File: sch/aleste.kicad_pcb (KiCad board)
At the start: 2 copper layers, 334 x 193 mm, 313 parts, among them P1 PIN, P2 PIN, P3 PIN, P4 PIN, P5 PIN, P6 PIN, P7 PIN, P8 PIN, Q1 16 MHz, Q2 13.333 MHz, Q3 QUARTZ, X1 SLOT-62, X2 CONN-7S, X3 CONN-5S, X4 SLOT-34, X5.A1 CONN-7S, X5.B1 CONN-7S, X6 CONN-7S, X7 CONN-7S, X8 CONN-12, X9 CONN-12

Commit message: More precise version. PCB needs a lot of work.
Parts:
- removed the CB1 at (45.7, 118.1)
- removed the CB1 at (316.2, 209.6)
- removed the CB1 at (316.2, 199.4)
- removed the CB1 at (316.2, 189.2)
- removed the CB1 at (316.2, 148.6)
- removed the CB1 at (316.2, 158.8)
- removed the CB1 at (316.2, 168.9)
- removed the CB1 at (316.2, 179.1)
- removed the CB1 at (341.6, 179.1)
- removed the CB1 at (341.6, 168.9)
- removed the CB1 at (341.6, 158.8)
- removed the CB1 at (92.7, 147.3)
- removed the CB1 at (341.6, 148.6)
- removed the CB1 at (341.6, 189.2)
- removed the CB1 at (341.6, 199.4)
- removed the CB1 at (341.6, 209.6)
- removed the CB1 at (341.6, 219.7)
- removed the CB1 at (290.8, 185.4)
- removed the CB1 at (44.5, 222.2)
- removed the CB1 at (38.1, 83.8)
- removed the CB1 at (110.5, 86.4)
- removed the CB1 at (44.5, 174.0)
- removed the CB1 at (38.1, 149.9)
- removed the CB1 at (145.4, 224.8)
- removed the CB1 at (294.6, 57.1)
- removed the CB1 at (309.9, 58.4)
- removed the CB1 at (256.5, 54.6)
- removed the CB1 at (243.8, 68.6)
- removed the CB1 at (316.2, 219.7)
- removed the P7 at (64.8, 118.1)
- removed the P7 at (64.8, 105.4)
- added CB1: CAP, MyLib_metric:C_Disc_D7.5_P2.5, F.Cu at (127.3, 86.1)
- added CB1: CAP, MyLib_metric:C_Disc_D7.5_P2.5, F.Cu at (331.0, 197.3)
- added CB1: CAP, MyLib_metric:C_Disc_D7.5_P2.5, F.Cu at (331.0, 187.3)
- added CB1: CAP, MyLib_metric:C_Disc_D7.5_P2.5, F.Cu at (331.0, 177.3)
- added CB1: CAP, MyLib_metric:C_Disc_D7.5_P2.5, F.Cu at (331.0, 167.3)
- added CB1: CAP, MyLib_metric:C_Disc_D7.5_P2.5, F.Cu at (331.0, 157.3)
- added CB1: CAP, MyLib_metric:C_Disc_D7.5_P2.5, F.Cu at (331.0, 147.3)
- added CB1: CAP, MyLib_metric:C_Disc_D7.5_P2.5, F.Cu at (356.0, 147.3)
- added CB1: CAP, MyLib_metric:C_Disc_D7.5_P2.5, F.Cu at (356.0, 157.3)
- added CB1: CAP, MyLib_metric:C_Disc_D7.5_P2.5, F.Cu at (356.0, 167.3)
- added CB1: CAP, MyLib_metric:C_Disc_D7.5_P2.5, F.Cu at (356.0, 177.3)
- added CB1: CAP, MyLib_metric:C_Disc_D7.5_P2.5, F.Cu at (56.0, 82.3)
- added CB1: CAP, MyLib_metric:C_Disc_D7.5_P2.5, F.Cu at (356.0, 187.3)
- added CB1: CAP, MyLib_metric:C_Disc_D7.5_P2.5, F.Cu at (356.0, 197.3)
- added CB1: CAP, MyLib_metric:C_Disc_D7.5_P2.5, F.Cu at (356.0, 207.3)
- added CB1: CAP, MyLib_metric:C_Disc_D7.5_P2.5, F.Cu at (356.0, 217.3)
- added CB1: CAP, MyLib_metric:C_Disc_D7.5_P2.5, F.Cu at (306.0, 184.8)
- added CB1: CAP, MyLib_metric:C_Disc_D7.5_P2.5, F.Cu at (259.8, 69.8)
- added CB1: CAP, MyLib_metric:C_Disc_D7.5_P2.5, F.Cu at (309.8, 57.3)
- added CB1: CAP, MyLib_metric:C_Disc_D7.5_P2.5, F.Cu at (324.8, 58.6)
- added CB1: CAP, MyLib_metric:C_Disc_D7.5_P2.5, F.Cu at (276.0, 172.3)
- added CB1: CAP, MyLib_metric:C_Disc_D7.5_P2.5, F.Cu at (162.3, 222.3)
- added CB1: CAP, MyLib_metric:C_Disc_D7.5_P2.5, F.Cu at (63.5, 117.3)
- added CB1: CAP, MyLib_metric:C_Disc_D7.5_P2.5, F.Cu at (62.3, 172.3)
- added CB1: CAP, MyLib_metric:C_Disc_D7.5_P2.5, F.Cu at (62.3, 222.3)
- added CB1: CAP, MyLib_metric:C_Disc_D7.5_P2.5, F.Cu at (113.5, 128.6)
- added CB1: CAP, MyLib_metric:C_Disc_D7.5_P2.5, F.Cu at (111.0, 146.1)
- added CB1: CAP, MyLib_metric:C_Disc_D7.5_P2.5, F.Cu at (56.0, 148.6)
- added CB1: CAP, MyLib_metric:C_Disc_D7.5_P2.5, F.Cu at (272.3, 54.8)
- added CB1: CAP, MyLib_metric:C_Disc_D7.5_P2.5, F.Cu at (331.0, 217.3)
- added CB1: CAP, MyLib_metric:C_Disc_D7.5_P2.5, F.Cu at (331.0, 207.3)
- added P7: PIN, MyLib:PIN, F.Cu at (82.3, 104.8)
- added P7: PIN, MyLib:PIN, F.Cu at (82.3, 117.3)
- added REF**: 1pin, Connect:1pin, F.Cu at (246.0, 51.1)
- added REF**: 1pin, Connect:1pin, F.Cu at (246.0, 221.1)
- added REF**: 1pin, Connect:1pin, F.Cu at (94.8, 221.1)
- added REF**: MountingHole_4-5mm, Mounting_Holes:MountingHole_4-5mm, F.Cu at (52.3, 46.1)
- C1, C2: value CAP -> 470; footprint MyLib:C_Disc_D7.5_P2.5 -> MyLib_metric:C_Disc_D7.5_P2.5
- C11, C12, C13, C15, C16, C17, C18, C23, C3, C4, C5, C7, C9: footprint MyLib:C_Disc_D7.5_P2.5 -> MyLib_metric:C_Disc_D7.5_P2.5
- D1, D10, D11, D12, D13, D14, D15, D16, D2, D20, D21, D22, D23, D24, D26, D28, D3, D32, D37, D38, D39, D4, D49, D5, D50, D51, D52, D53, D54, D55, D56, D59, D6, D63, D64, D67, D68, D69, D7, D74, D79, D8, D80, D81, D87, D88, D9: footprint MyLib:DIP-16 -> MyLib_metric:DIP-16
- D17, D18, D25, D30, D70: footprint MyLib:DIP-40 -> MyLib_metric:DIP-40
- D19, D33, D60, D61, D62, D65, D82, D83: footprint MyLib:DIP-24 -> MyLib_metric:DIP-24
- D29, D35, D36, D40, D41, D42, D43, D44, D57, D66, D71, D72, D73, D75, D76, D77, D78, D85: footprint MyLib:DIP-14 -> MyLib_metric:DIP-14
- D31, D34: footprint MyLib:DIP-28 -> MyLib_metric:DIP-28
- D45, D46, D47, D48, D58, D84, D89: footprint MyLib:DIP-20 -> MyLib_metric:DIP-20
- D86: footprint MyLib:DIP-8 -> MyLib_metric:DIP-8
- Q3: footprint MyLib:Crystal_Round_Vertical_5mm -> MyLib_metric:Crystal_Round_Vertical_5mm
- R1, R100, R105, R2, R3, R36, R4, R59, R60, R61: value RES -> 1.2K; footprint MyLib:Resistor_Horizontal_RM7.5mm -> MyLib_metric:Resistor_Horizontal_RM7.5mm
- R10, R106, R107, R108, R109, R11, R110, R111, R112, R113, R12, R13, R17, R18, R19, R20, R21, R22, R23, R28, R29, R30, R31, R32, R47, R48, R49, R50, R88, R89, R90, R91, R92, R93, R94, R95: footprint MyLib:Resistor_Vertical_RM2.5mm -> MyLib_metric:Resistor_Vertical_RM2.5mm
- R101, R102, R16, R57: value RES -> 360; footprint MyLib:Resistor_Horizontal_RM7.5mm -> MyLib_metric:Resistor_Horizontal_RM7.5mm
- R114, R115, R116, R117, R118, R119, R120, R121, R122: value RES -> 27; footprint MyLib:Resistor_Horizontal_RM7.5mm -> MyLib_metric:Resistor_Horizontal_RM7.5mm
- R123, R134, R136, R15, R35, R37, R38, R5, R52, R53, R54, R55, R58: footprint MyLib:Resistor_Horizontal_RM7.5mm -> MyLib_metric:Resistor_Horizontal_RM7.5mm
- R126, R127, R128, R131, R132, R133, R14, R25, R76, R82, R83, R84, R85, R86, R87: value RES -> 2K; footprint MyLib:Resistor_Horizontal_RM7.5mm -> MyLib_metric:Resistor_Horizontal_RM7.5mm
- R129: value RES -> 510; footprint MyLib:Resistor_Horizontal_RM7.5mm -> MyLib_metric:Resistor_Horizontal_RM7.5mm
- R130, R62, R63, R64, R66, R81: value RES -> 220; footprint MyLib:Resistor_Horizontal_RM7.5mm -> MyLib_metric:Resistor_Horizontal_RM7.5mm
- R135, R27, R33: value RES -> 10K; footprint MyLib:Resistor_Horizontal_RM7.5mm -> MyLib_metric:Resistor_Horizontal_RM7.5mm
- R24, R39, R40, R41, R42, R43, R44, R45, R46, R7, R77, R78, R79, R8, R80, R9: value RES -> 51; footprint MyLib:Resistor_Horizontal_RM7.5mm -> MyLib_metric:Resistor_Horizontal_RM7.5mm
- R26, R34: value RES -> 10k; footprint MyLib:Resistor_Horizontal_RM7.5mm -> MyLib_metric:Resistor_Horizontal_RM7.5mm
- R51: value RES -> 1.2k; footprint MyLib:Resistor_Horizontal_RM7.5mm -> MyLib_metric:Resistor_Horizontal_RM7.5mm
- R56, R65: value RES -> 120; footprint MyLib:Resistor_Horizontal_RM7.5mm -> MyLib_metric:Resistor_Horizontal_RM7.5mm
- R6: value RES -> 15K; footprint MyLib:Resistor_Horizontal_RM7.5mm -> MyLib_metric:Resistor_Horizontal_RM7.5mm
- R67, R68, R69, R70: value RES -> 2K; footprint MyLib:Resistor_Vertical_RM2.5mm -> MyLib_metric:Resistor_Vertical_RM2.5mm
- R71, R72, R73, R74, R75: value RES -> 1.2K; footprint MyLib:Resistor_Vertical_RM2.5mm -> MyLib_metric:Resistor_Vertical_RM2.5mm
- VD1, VD10, VD11, VD12, VD13, VD14, VD2, VD4, VD5, VD6, VD7, VD8, VD9: footprint MyLib:Diode_DO-35_SOD27_Horizontal_RM7.5 -> MyLib_metric:Diode_DO-35_SOD27_Horizontal_RM7.5
- X8, X9: footprint MyLib:FB-12 -> MyLib_metric:FB-12
- moved D30 42.0 mm to (182.3, 68.6)
- moved D25 40.9 mm to (258.5, 111.1)
- moved D70 40.1 mm to (313.5, 111.1)
- moved D31 34.7 mm to (174.8, 89.8)
- moved D17 33.8 mm to (142.3, 94.8)
- moved D33 32.1 mm to (113.5, 118.6)
- moved D34 31.9 mm to (361.0, 111.1)
- moved X9 30.3 mm to (237.3, 81.1)
- moved D63 27.1 mm to (72.3, 162.3)
- moved D64 26.7 mm to (94.8, 162.3)
- moved D78 26.2 mm to (122.3, 146.1)
- moved D77 26.2 mm to (122.3, 134.8)
- moved D24 26.0 mm to (209.8, 89.8)
- moved D39 25.7 mm to (253.5, 212.3)
- moved D37 25.6 mm to (253.5, 199.8)
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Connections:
- D18 pad 26: (no net) -> Net-(D18-Pad26)
- D18 pad 39: (no net) -> Net-(D18-Pad39)
- D19 pad 19: (no net) -> Net-(D19-Pad19)
- D19 pad 21: (no net) -> Net-(D19-Pad21)
- D19 pad 23: (no net) -> Net-(D19-Pad23)
- D24 pad 6: (no net) -> Net-(D24-Pad6)
- D25 pad 15: (no net) -> Net-(D25-Pad15)
- D25 pad 34: (no net) -> Net-(D25-Pad34)
- D25 pad 35: (no net) -> Net-(D25-Pad35)
- D34 pad 14: (no net) -> Net-(D34-Pad14)
- D34 pad 15: (no net) -> Net-(D34-Pad15)
- D34 pad 16: (no net) -> Net-(D34-Pad16)
- D34 pad 17: (no net) -> Net-(D34-Pad17)
- D34 pad 18: (no net) -> Net-(D34-Pad18)
- D34 pad 23: (no net) -> Net-(D34-Pad23)
- D37 pad 15: (no net) -> Net-(D37-Pad15)
- D37 pad 3: (no net) -> Net-(D37-Pad3)
- D37 pad 4: (no net) -> Net-(D37-Pad4)
- D37 pad 5: (no net) -> Net-(D37-Pad5)
- D37 pad 6: (no net) -> Net-(D37-Pad6)
- D39 pad 2: (no net) -> Net-(D39-Pad2)
- D39 pad 7: (no net) -> Net-(D39-Pad7)
- D40 pad 11: (no net) -> /RAM/MVI
- D40 pad 5: (no net) -> Net-(D40-Pad5)
- D49 pad 2: (no net) -> Net-(D49-Pad2)
- D49 pad 7: (no net) -> Net-(D49-Pad7)
- D50 pad 13: (no net) -> Net-(D50-Pad13)
- D50 pad 15: (no net) -> Net-(D50-Pad15)
- D50 pad 2: (no net) -> Net-(D50-Pad2)
- D50 pad 7: (no net) -> Net-(D50-Pad7)
- D51 pad 13: (no net) -> Net-(D51-Pad13)
- D51 pad 15: (no net) -> Net-(D51-Pad15)
- D51 pad 7: (no net) -> Net-(D51-Pad7)
- D54 pad 4: (no net) -> Net-(D54-Pad4)
- D54 pad 5: (no net) -> Net-(D54-Pad5)
- D54 pad 7: (no net) -> Net-(D54-Pad7)
- D56 pad 14: (no net) -> Net-(D56-Pad14)
- D56 pad 15: (no net) -> Net-(D56-Pad15)
- D57 pad 6: (no net) -> Net-(D57-Pad6)
- D57 pad 8: (no net) -> Net-(D57-Pad8)
- D58 pad 16: (no net) -> Net-(D58-Pad16)
- D58 pad 17: (no net) -> Net-(D58-Pad17)
- D58 pad 18: (no net) -> Net-(D58-Pad18)
- D58 pad 19: (no net) -> Net-(D58-Pad19)
- D60 pad 17: (no net) -> Net-(D60-Pad17)
- D60 pad 8: (no net) -> Net-(D60-Pad8)
- D61 pad 17: (no net) -> Net-(D61-Pad17)
- D61 pad 8: (no net) -> Net-(D61-Pad8)
- D62 pad 16: (no net) -> Net-(D62-Pad16)
- D63 pad 12: (no net) -> Net-(D63-Pad12)
- D63 pad 13: (no net) -> Net-(D63-Pad13)
- D63 pad 14: (no net) -> Net-(D63-Pad14)
- D64 pad 11: (no net) -> Net-(D64-Pad11)
- D65 pad 13: (no net) -> Net-(D65-Pad13)
- D69 pad 6: (no net) -> Net-(D69-Pad6)
- D69 pad 7: (no net) -> Net-(D69-Pad7)
- D69 pad 9: (no net) -> Net-(D69-Pad9)
- D70 pad 14: (no net) -> Net-(D70-Pad14)
- D70 pad 24: (no net) -> Net-(D70-Pad24)
- D70 pad 26: (no net) -> Net-(D70-Pad26)
- D70 pad 31: (no net) -> Net-(D70-Pad31)
- D70 pad 32: (no net) -> Net-(D70-Pad32)
- D70 pad 36: (no net) -> Net-(D70-Pad36)
- D71 pad 8: (no net) -> Net-(D71-Pad8)
- D74 pad 11: (no net) -> Net-(D74-Pad11)
- D74 pad 12: (no net) -> Net-(D74-Pad12)
- D74 pad 4: (no net) -> Net-(D74-Pad4)
- D74 pad 5: (no net) -> Net-(D74-Pad5)
- D74 pad 6: (no net) -> Net-(D74-Pad6)
- D77 pad 6: (no net) -> Net-(D77-Pad6)
- D79 pad 14: (no net) -> Net-(D79-Pad14)
- D79 pad 15: (no net) -> Net-(D79-Pad15)
- D81 pad 6: (no net) -> Net-(D81-Pad6)
- D88 pad 1: (no net) -> Net-(D88-Pad1)
- D88 pad 2: (no net) -> Net-(D88-Pad2)
- D88 pad 7: (no net) -> Net-(D88-Pad7)
- D88 pad 9: (no net) -> Net-(D88-Pad9)
- D89 pad 11: (no net) -> Net-(D89-Pad11)
- D89 pad 12: (no net) -> Net-(D89-Pad12)
- D89 pad 13: (no net) -> Net-(D89-Pad13)
- D89 pad 7: (no net) -> Net-(D89-Pad7)
- D89 pad 8: (no net) -> Net-(D89-Pad8)
- D89 pad 9: (no net) -> Net-(D89-Pad9)
- X1 pad B20: (no net) -> Net-(X1-PadB20)
- X1 pad B24: (no net) -> /~EXP
- X4 pad A1: (no net) -> Net-(X4-PadA1)
- X4 pad A17: (no net) -> Net-(X4-PadA17)
- X4 pad A2: (no net) -> Net-(X4-PadA2)
- X4 pad A3: (no net) -> Net-(X4-PadA3)
- X4 pad A7: (no net) -> Net-(X4-PadA7)
- X9 pad 10: (no net) -> Net-(X9-Pad10)
- X9 pad 11: (no net) -> Net-(X9-Pad11)
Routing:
- net GND: track 4808.9 -> 0.00 mm, vias 51 -> 0
- net VCC: track 3489.0 -> 0.00 mm, vias 37 -> 0
- net /CPU/~IOWR: track 727.8 -> 0.00 mm, vias 9 -> 0
- net /CPU/D3: track 648.1 -> 0.00 mm, vias 17 -> 0
- net /CPU/HY: track 639.2 -> 0.00 mm, vias 6 -> 0
- net /CPU/D4: track 630.6 -> 0.00 mm, vias 13 -> 0
- net /CPU/D0: track 599.5 -> 0.00 mm, vias 9 -> 0
- net /CPU/D1: track 598.1 -> 0.00 mm, vias 15 -> 0
- net /CPU/D2: track 572.5 -> 0.00 mm, vias 9 -> 0
- net /CPU/D6: track 550.3 -> 0.00 mm, vias 10 -> 0
- net /CPU/D7: track 548.0 -> 0.00 mm, vias 12 -> 0
- net /CPU/D5: track 530.0 -> 0.00 mm, vias 14 -> 0
- net /FDC/XD0: track 525.6 -> 0.00 mm, vias 7 -> 0
- net /CPU/~IORD: track 503.3 -> 0.00 mm, vias 9 -> 0
- net /CPU/A8: track 502.3 -> 0.00 mm, vias 10 -> 0
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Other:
- board size 334 x 193 mm -> 330 x 190 mm
- net class Default: via_dia 1 -> 1.2; via_drill 0.5 -> 0.8
- rule pad_to_mask_clearance: 0.2 -> 0
- board text removed: "Aleste 520EX"
- board text removed: "PATISONIC ALESTE 520 EX 01.003"
- board text removed: "designed by Patisonic, Omsk, 1992-1993 restored by Alexander Molodtsov, 2015"

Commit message: Board fully redrawn
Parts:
- C10, C14, C22: value CAPP -> 100мк
- C11: value CAP -> 12
- C12: value CAP -> 24
- C13: value CAP -> 47н
- C20: value CAPP -> 1000мк
- C23: value CAP -> 0,47мк
- C24, C6: value CAPP -> 1мк
- C25, C26: value CAPP -> 47мк
- C7: value CAP -> 0,33мк
- C9: value CAP -> 1,5мк
- CB1: value CAP -> 0,1мк
- DR1: value INDUCTOR -> 91мкГ
- DR2: value INDUCTOR -> 51мкГ
- R1, R100, R105, R2, R3, R36, R4, R60, R71, R72, R73, R74, R75: value 1.2K -> 1,2к
- R10, R11, R12, R13, R28, R29, R30, R31, R32, R47, R48, R49, R50: value RES -> 1,2к
- R106, R107, R108, R109, R110, R111, R112, R113, R17, R18, R19, R20, R21, R22, R23, R88, R89, R90, R91, R92, R93, R94, R95: value RES -> 10к
- R123, R15, R5: value RES -> 2,7к
- R126, R132, R14, R25, R67, R68, R69, R70, R76, R82, R83, R84, R85, R86, R87: value 2K -> 2,7к
- R127, R131: value 2K -> 6,8к
- R128, R133: value 2K -> 3,3к
- R134, R53, R55: value RES -> 360
- R135, R27, R33: value 10K -> 10к
- R35: value RES -> 390к
- R37: value RES -> 10М
- R38: value RES -> 470к
- R51: value 1.2k -> 1,2к
- R52, R54: value RES -> 200
- R56: value 120 -> 200
- R58: value RES -> 510
- R59: value 1.2K -> 6,8к
- R6: value 15K -> 2,7к
- R61: value 1.2K -> 3,3к
- moved C26 2.50 mm to (352.3, 77.3)
- moved CB1 2.50 mm to (62.3, 219.8)
- moved D59 2.50 mm to (62.3, 207.3)
- moved CB1 2.25 mm to (304.1, 183.6)
- moved CB1 2.25 mm to (111.6, 129.8)
- moved D45 2.25 mm to (296.6, 199.8)
- moved D46 2.25 mm to (311.6, 199.8)
- moved D47 2.25 mm to (296.6, 167.3)
- moved D48 2.25 mm to (311.6, 167.3)
- moved R77 2.25 mm to (311.6, 219.8)
- moved R78 2.25 mm to (296.6, 214.8)
- moved R79 2.25 mm to (296.6, 217.3)
- moved R8 2.25 mm to (311.6, 214.8)
- moved R80 2.25 mm to (296.6, 219.8)
- moved R9 2.25 mm to (311.6, 217.3)
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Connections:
- net /CPU/A0 renamed /A0
- net /CPU/A1 renamed /A1
- net /CPU/A10 renamed /A10
- net /CPU/A11 renamed /A11
- net /CPU/A12 renamed /A12
- net /CPU/A13 renamed /A13
- net /CPU/A14 renamed /A14
- net /CPU/A15 renamed /A15
- net /CPU/A2 renamed /A2
- net /CPU/A3 renamed /A3
- net /CPU/A4 renamed /A4
- net /CPU/A5 renamed /A5
- net /CPU/A6 renamed /A6
- net /CPU/A7 renamed /A7
- net /CPU/A8 renamed /A8
- net /CPU/A9 renamed /A9
- net /CPU/BUFFER0 renamed /BUFFER0
- net /CPU/BUFFER1 renamed /BUFFER1
- net /CPU/CLK renamed /CLK
- net /CPU/D0 renamed /D0
- net /CPU/D1 renamed /D1
- net /CPU/D2 renamed /D2
- net /CPU/D3 renamed /D3
- net /CPU/D4 renamed /D4
- net /CPU/D5 renamed /D5
- net /CPU/D6 renamed /D6
- net /CPU/D7 renamed /D7
- net /CPU/HY renamed /HY
- net /CPU/PROM0 renamed /PROM0
- net /CPU/PROM1 renamed /PROM1
- net /CPU/RAMDIS renamed /RAMDIS
- net /CPU/ROM0 renamed /ROM0
- net /CPU/ROM1 renamed /ROM1
- net /CPU/ROMDIS renamed /ROMDIS
- net /CPU/SINT renamed /SINT
- net /CPU/~BUSAK renamed /~BUSAK
- net /CPU/~BUSRQ renamed /~BUSRQ
- net /CPU/~HALT renamed /~HALT
- net /CPU/~INT renamed /~INT
- net /CPU/~INTA renamed /~INTA
- net /CPU/~IORD renamed /~IORD
- net /CPU/~IORQ renamed /~IORQ
- net /CPU/~IOWR renamed /~IOWR
- net /CPU/~M1 renamed /~M1
- net /CPU/~MREQ renamed /~MREQ
- net /CPU/~NMI renamed /~NMI
- net /CPU/~RAMEN renamed /~RAMEN
- net /CPU/~RD renamed /~RD
- net /CPU/~RESET renamed /~RESET
- net /CPU/~RFSH renamed /~RFSH
- net /CPU/~ROMEN renamed /~ROMEN
- net /CPU/~WAIT renamed /~WAIT
- net /CPU/~WR renamed /~WR
- net /Clocks & CRTC/16MHZ renamed /16MHZ
- net /Clocks & CRTC/1CY renamed /1CY
- net /Clocks & CRTC/1M renamed /1M
- net /Clocks & CRTC/2CY renamed /2CY
- net /Clocks & CRTC/2M renamed /2M
- net /Clocks & CRTC/3CY renamed /3CY
- net /Clocks & CRTC/4M renamed /4M
- net /Clocks & CRTC/8M renamed /8M
- net /Clocks & CRTC/CAS renamed /CAS
- net /Clocks & CRTC/CBUF renamed /CBUF
- net /Clocks & CRTC/CURSOR renamed /CURSOR
- net /Clocks & CRTC/DEN renamed /DEN
- net /Clocks & CRTC/HIGHT renamed /HIGHT
- net /Clocks & CRTC/HX renamed /HX
- net /Clocks & CRTC/HY* renamed /HY*
- net /Clocks & CRTC/KK0 renamed /KK0
- net /Clocks & CRTC/KK1 renamed /KK1
- net /Clocks & CRTC/KK2 renamed /KK2
- net /Clocks & CRTC/KK3 renamed /KK3
- net /Clocks & CRTC/L.PEN renamed /L.PEN
- net /Clocks & CRTC/L0 renamed /L0
- net /Clocks & CRTC/L1 renamed /L1
- net /Clocks & CRTC/L2 renamed /L2
- net /Clocks & CRTC/MK0 renamed /MK0
- net /Clocks & CRTC/MK1 renamed /MK1
- net /Clocks & CRTC/MK2 renamed /MK2
- net /Clocks & CRTC/MK3 renamed /MK3
- net /Clocks & CRTC/RAS renamed /RAS
- net /Clocks & CRTC/SINT* renamed /SINT*
- net /Clocks & CRTC/SYNC* renamed /SYNC*
- net /Clocks & CRTC/V1 renamed /V1
- net /Clocks & CRTC/V10 renamed /V10
- net /Clocks & CRTC/V1113 renamed /V1113
- net /Clocks & CRTC/V14 renamed /V14
- net /Clocks & CRTC/V2 renamed /V2
- net /Clocks & CRTC/V3 renamed /V3
- net /Clocks & CRTC/V4 renamed /V4
- net /Clocks & CRTC/V5 renamed /V5
- net /Clocks & CRTC/V6 renamed /V6
- net /Clocks & CRTC/V7 renamed /V7
- net /Clocks & CRTC/V8 renamed /V8
- net /Clocks & CRTC/V9 renamed /V9
- net /Clocks & CRTC/VCLK renamed /VCLK
- net /Clocks & CRTC/XTAL renamed /XTAL
- net /Clocks & CRTC/~3CY renamed /~3CY
- net /FDC/DISCINT renamed /DISCINT
- net /FDC/DW renamed /DW
- net /FDC/EXRG renamed /EXRG
- net /FDC/RESET renamed /RESET
- net /FDC/RSCLK renamed /RSCLK
- net /FDC/WGPTCLK renamed /WGPTCLK
- net /FDC/XD0 renamed /XD0
- net /Gate Array/CS53 renamed /CS53
- net /Gate Array/HIGHTZ renamed /HIGHTZ
- net /Gate Array/M4 renamed /M4
- net /Gate Array/MAP14 renamed /MAP14
- net /Gate Array/MAP15 renamed /MAP15
- net /Gate Array/MAP16 renamed /MAP16
- net /Gate Array/MAP17 renamed /MAP17
- net /Gate Array/MAP18 renamed /MAP18
- net /Gate Array/MAPBLK renamed /MAPBLK
- net /Gate Array/SOUND renamed /SOUND
- net /Gate Array/VD0 renamed /VD0
- net /Gate Array/VD1 renamed /VD1
- net /Gate Array/VD2 renamed /VD2
- net /Gate Array/VD3 renamed /VD3
- net /Gate Array/VD4 renamed /VD4
- net /Gate Array/VD5 renamed /VD5
- net /Gate Array/VD6 renamed /VD6
- net /Gate Array/VD7 renamed /VD7
- net /Gate Array/~CSAY renamed /~CSAY
- net /Gate Array/~FUTURE renamed /~FUTURE
- net /RAM/DIS renamed /DIS
- net /RAM/~DIS renamed /~DIS
- D18 pad 26: Net-(D18-Pad26) -> (no net)
- D18 pad 39: Net-(D18-Pad39) -> (no net)
- D19 pad 19: Net-(D19-Pad19) -> (no net)
- D19 pad 21: Net-(D19-Pad21) -> (no net)
- D19 pad 23: Net-(D19-Pad23) -> (no net)
- D24 pad 6: Net-(D24-Pad6) -> (no net)
- D25 pad 15: Net-(D25-Pad15) -> (no net)
- D25 pad 34: Net-(D25-Pad34) -> (no net)
- D25 pad 35: Net-(D25-Pad35) -> (no net)
- D34 pad 14: Net-(D34-Pad14) -> (no net)
- D34 pad 15: Net-(D34-Pad15) -> (no net)
- D34 pad 16: Net-(D34-Pad16) -> (no net)
- D34 pad 17: Net-(D34-Pad17) -> (no net)
- D34 pad 18: Net-(D34-Pad18) -> (no net)
- D34 pad 23: Net-(D34-Pad23) -> (no net)
- D35 pad 6: /Gate Array/MVI -> /MVI
- D37 pad 15: Net-(D37-Pad15) -> (no net)
- D37 pad 3: Net-(D37-Pad3) -> (no net)
- D37 pad 4: Net-(D37-Pad4) -> (no net)
- D37 pad 5: Net-(D37-Pad5) -> (no net)
- D37 pad 6: Net-(D37-Pad6) -> (no net)
- D39 pad 2: Net-(D39-Pad2) -> (no net)
- D39 pad 7: Net-(D39-Pad7) -> (no net)
- D40 pad 11: /RAM/MVI -> /MVI
- D40 pad 5: Net-(D40-Pad5) -> (no net)
- D49 pad 10: /Gate Array/MVI -> /MVI
- D49 pad 2: Net-(D49-Pad2) -> (no net)
- D49 pad 7: Net-(D49-Pad7) -> (no net)
- D49 pad 9: /Gate Array/MVI -> /MVI
- D50 pad 10: /Gate Array/MVI -> /MVI
- D50 pad 13: Net-(D50-Pad13) -> (no net)
- D50 pad 15: Net-(D50-Pad15) -> (no net)
- D50 pad 2: Net-(D50-Pad2) -> (no net)
- D50 pad 7: Net-(D50-Pad7) -> (no net)
- D51 pad 10: /Gate Array/MVI -> /MVI
- D51 pad 13: Net-(D51-Pad13) -> (no net)
- D51 pad 15: Net-(D51-Pad15) -> (no net)
- D51 pad 7: Net-(D51-Pad7) -> (no net)
- D54 pad 4: Net-(D54-Pad4) -> (no net)
- D54 pad 5: Net-(D54-Pad5) -> (no net)
- D54 pad 7: Net-(D54-Pad7) -> (no net)
- D56 pad 14: Net-(D56-Pad14) -> (no net)
- D56 pad 15: Net-(D56-Pad15) -> (no net)
- D57 pad 6: Net-(D57-Pad6) -> (no net)
- D57 pad 8: Net-(D57-Pad8) -> (no net)
- D58 pad 16: Net-(D58-Pad16) -> (no net)
- D58 pad 17: Net-(D58-Pad17) -> (no net)
- D58 pad 18: Net-(D58-Pad18) -> (no net)
- D58 pad 19: Net-(D58-Pad19) -> (no net)
- D60 pad 17: Net-(D60-Pad17) -> (no net)
- D60 pad 8: Net-(D60-Pad8) -> (no net)
- D61 pad 17: Net-(D61-Pad17) -> (no net)
- D61 pad 8: Net-(D61-Pad8) -> (no net)
- D62 pad 16: Net-(D62-Pad16) -> (no net)
- D63 pad 12: Net-(D63-Pad12) -> (no net)
- D63 pad 13: Net-(D63-Pad13) -> (no net)
- D63 pad 14: Net-(D63-Pad14) -> (no net)
- D64 pad 11: Net-(D64-Pad11) -> (no net)
- D65 pad 13: Net-(D65-Pad13) -> (no net)
- D69 pad 6: Net-(D69-Pad6) -> (no net)
- D69 pad 7: Net-(D69-Pad7) -> (no net)
- D69 pad 9: Net-(D69-Pad9) -> (no net)
- D70 pad 14: Net-(D70-Pad14) -> (no net)
- D70 pad 24: Net-(D70-Pad24) -> (no net)
- D70 pad 26: Net-(D70-Pad26) -> (no net)
- D70 pad 31: Net-(D70-Pad31) -> (no net)
- D70 pad 32: Net-(D70-Pad32) -> (no net)
- D70 pad 36: Net-(D70-Pad36) -> (no net)
- D71 pad 8: Net-(D71-Pad8) -> (no net)
- D74 pad 11: Net-(D74-Pad11) -> (no net)
- D74 pad 12: Net-(D74-Pad12) -> (no net)
- D74 pad 4: Net-(D74-Pad4) -> (no net)
- D74 pad 5: Net-(D74-Pad5) -> (no net)
- D74 pad 6: Net-(D74-Pad6) -> (no net)
- D77 pad 6: Net-(D77-Pad6) -> (no net)
- D79 pad 14: Net-(D79-Pad14) -> (no net)
- D79 pad 15: Net-(D79-Pad15) -> (no net)
- D81 pad 6: Net-(D81-Pad6) -> (no net)
- D88 pad 1: Net-(D88-Pad1) -> (no net)
- D88 pad 2: Net-(D88-Pad2) -> (no net)
- D88 pad 7: Net-(D88-Pad7) -> (no net)
- D88 pad 9: Net-(D88-Pad9) -> (no net)
- D89 pad 11: Net-(D89-Pad11) -> (no net)
- D89 pad 12: Net-(D89-Pad12) -> (no net)
- D89 pad 13: Net-(D89-Pad13) -> (no net)
- D89 pad 7: Net-(D89-Pad7) -> (no net)
- D89 pad 8: Net-(D89-Pad8) -> (no net)
- D89 pad 9: Net-(D89-Pad9) -> (no net)
- R76 pad 1: VCC -> Net-(D70-Pad15)
- R76 pad 2: Net-(D70-Pad15) -> VCC
- X1 pad B20: Net-(X1-PadB20) -> (no net)
- X1 pad B24: /~EXP -> (no net)
- X4 pad A1: Net-(X4-PadA1) -> (no net)
- X4 pad A17: Net-(X4-PadA17) -> (no net)
- X4 pad A2: Net-(X4-PadA2) -> (no net)
- X4 pad A3: Net-(X4-PadA3) -> (no net)
- X4 pad A7: Net-(X4-PadA7) -> (no net)
- X9 pad 10: Net-(X9-Pad10) -> (no net)
- X9 pad 11: Net-(X9-Pad11) -> (no net)
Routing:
- net GND: track 0.00 -> 4144.7 mm, vias 0 -> 47
- net VCC: track 0.00 -> 3431.0 mm, vias 0 -> 30
- net /D3: track 0.00 -> 647.9 mm, vias 0 -> 17
- net /D4: track 0.00 -> 621.7 mm, vias 0 -> 13
- net /D1: track 0.00 -> 589.3 mm, vias 0 -> 15
- net /D0: track 0.00 -> 588.6 mm, vias 0 -> 9
- net /D2: track 0.00 -> 563.6 mm, vias 0 -> 9
- net /D7: track 0.00 -> 544.8 mm, vias 0 -> 12
- net /D6: track 0.00 -> 541.9 mm, vias 0 -> 10
- net /D5: track 0.00 -> 534.6 mm, vias 0 -> 14
- net /XD0: track 0.00 -> 528.3 mm, vias 0 -> 7
- net /~IOWR: track 0.00 -> 527.2 mm, vias 0 -> 9
- net /~IORD: track 0.00 -> 492.9 mm, vias 0 -> 9
- net /A8: track 0.00 -> 492.2 mm, vias 0 -> 10
- net /A0: track 0.00 -> 415.2 mm, vias 0 -> 11
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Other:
- board size 330 x 190 mm -> 328.8 x 190 mm
- board text added: "Aleste 520EX"
- board text added: "TIN"
- board text added: "TOUT"
- board text added: "WGPTCLK"
- board text added: "designed by Patisonic, Omsk, 1992-1993"
- board text added: "restored by Alexander Molodtsov, 2015"

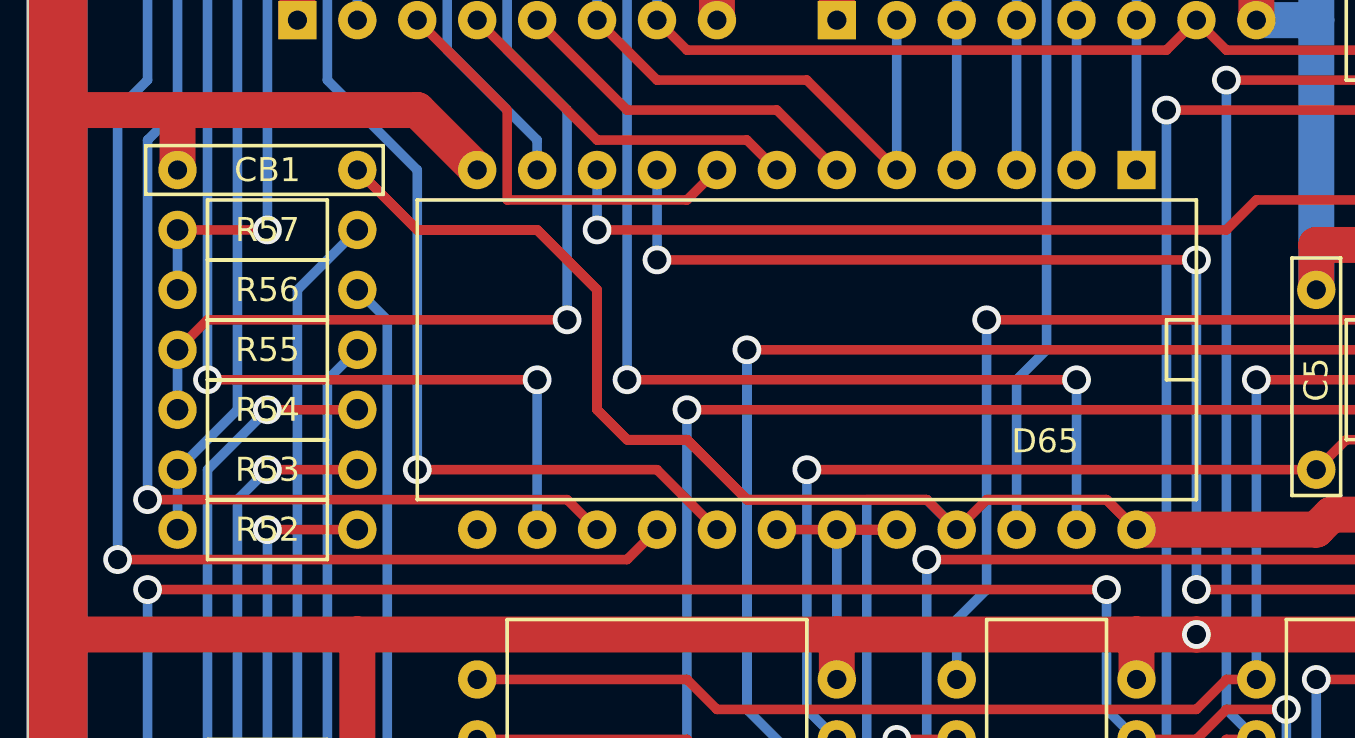
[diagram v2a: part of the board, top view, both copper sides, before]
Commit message: C8 on its place
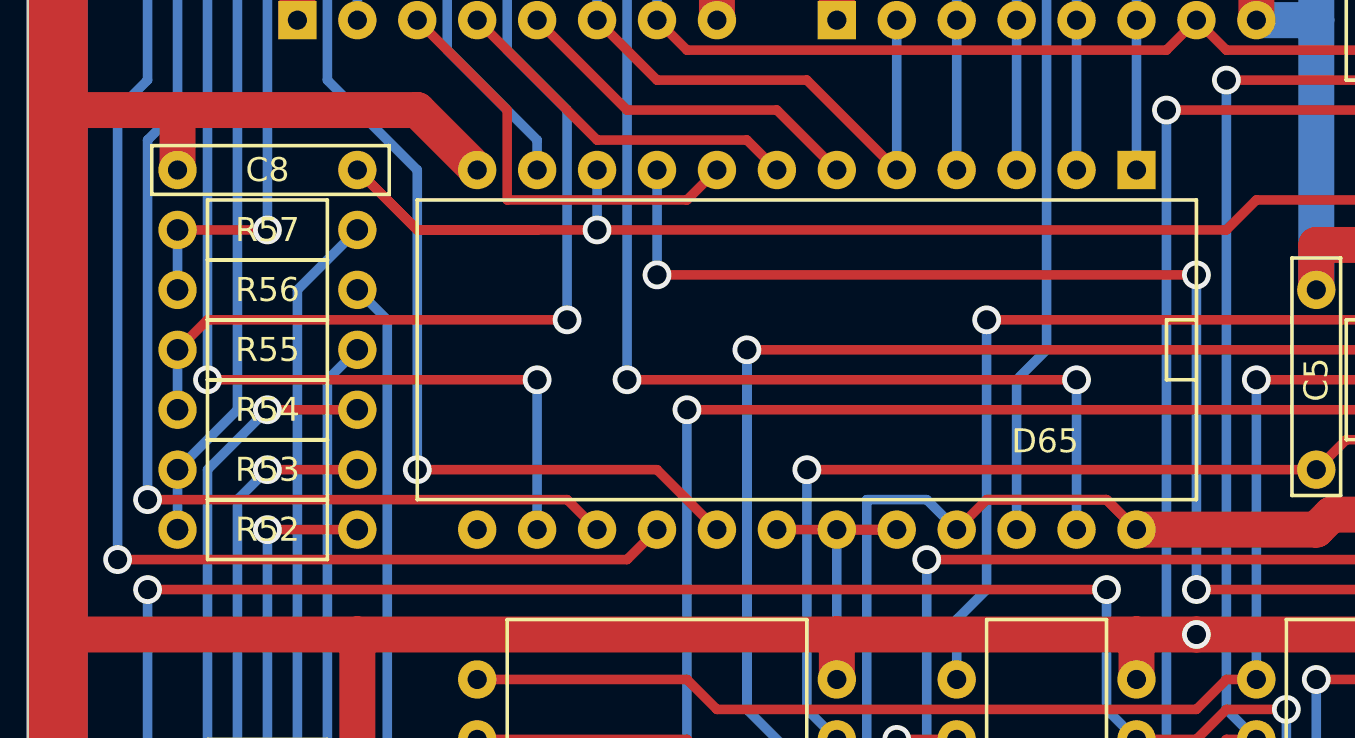
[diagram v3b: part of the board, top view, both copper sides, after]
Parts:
- C8: renamed from CB1; value CAP -> 1н
- turned C8 to 180 degrees
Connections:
- C8 pad 1: GND -> /HY*
- C8 pad 2: VCC -> GND
- D18 pad 26: (no net) -> Net-(D18-Pad26)
- D18 pad 39: (no net) -> Net-(D18-Pad39)
- D19 pad 19: (no net) -> Net-(D19-Pad19)
- D19 pad 21: (no net) -> Net-(D19-Pad21)
- D19 pad 23: (no net) -> Net-(D19-Pad23)
- D24 pad 6: (no net) -> Net-(D24-Pad6)
- D25 pad 15: (no net) -> Net-(D25-Pad15)
- D25 pad 34: (no net) -> Net-(D25-Pad34)
- D25 pad 35: (no net) -> Net-(D25-Pad35)
- D34 pad 14: (no net) -> Net-(D34-Pad14)
- D34 pad 15: (no net) -> Net-(D34-Pad15)
- D34 pad 16: (no net) -> Net-(D34-Pad16)
- D34 pad 17: (no net) -> Net-(D34-Pad17)
- D34 pad 18: (no net) -> Net-(D34-Pad18)
- D34 pad 23: (no net) -> Net-(D34-Pad23)
- D37 pad 15: (no net) -> Net-(D37-Pad15)
- D37 pad 3: (no net) -> Net-(D37-Pad3)
- D37 pad 4: (no net) -> Net-(D37-Pad4)
- D37 pad 5: (no net) -> Net-(D37-Pad5)
- D37 pad 6: (no net) -> Net-(D37-Pad6)
- D39 pad 2: (no net) -> Net-(D39-Pad2)
- D39 pad 7: (no net) -> Net-(D39-Pad7)
- D40 pad 5: (no net) -> Net-(D40-Pad5)
- D49 pad 2: (no net) -> Net-(D49-Pad2)
- D49 pad 7: (no net) -> Net-(D49-Pad7)
- D50 pad 13: (no net) -> Net-(D50-Pad13)
- D50 pad 15: (no net) -> Net-(D50-Pad15)
- D50 pad 2: (no net) -> Net-(D50-Pad2)
- D50 pad 7: (no net) -> Net-(D50-Pad7)
- D51 pad 13: (no net) -> Net-(D51-Pad13)
- D51 pad 15: (no net) -> Net-(D51-Pad15)
- D51 pad 7: (no net) -> Net-(D51-Pad7)
- D54 pad 4: (no net) -> Net-(D54-Pad4)
- D54 pad 5: (no net) -> Net-(D54-Pad5)
- D54 pad 7: (no net) -> Net-(D54-Pad7)
- D56 pad 14: (no net) -> Net-(D56-Pad14)
- D56 pad 15: (no net) -> Net-(D56-Pad15)
- D57 pad 6: (no net) -> Net-(D57-Pad6)
- D57 pad 8: (no net) -> Net-(D57-Pad8)
- D58 pad 16: (no net) -> Net-(D58-Pad16)
- D58 pad 17: (no net) -> Net-(D58-Pad17)
- D58 pad 18: (no net) -> Net-(D58-Pad18)
- D58 pad 19: (no net) -> Net-(D58-Pad19)
- D60 pad 17: (no net) -> Net-(D60-Pad17)
- D60 pad 8: (no net) -> Net-(D60-Pad8)
- D61 pad 17: (no net) -> Net-(D61-Pad17)
- D61 pad 8: (no net) -> Net-(D61-Pad8)
- D62 pad 16: (no net) -> Net-(D62-Pad16)
- D63 pad 12: (no net) -> Net-(D63-Pad12)
- D63 pad 13: (no net) -> Net-(D63-Pad13)
- D63 pad 14: (no net) -> Net-(D63-Pad14)
- D64 pad 11: (no net) -> Net-(D64-Pad11)
- D65 pad 13: (no net) -> Net-(D65-Pad13)
- D69 pad 6: (no net) -> Net-(D69-Pad6)
- D69 pad 7: (no net) -> Net-(D69-Pad7)
- D69 pad 9: (no net) -> Net-(D69-Pad9)
- D70 pad 14: (no net) -> Net-(D70-Pad14)
- D70 pad 24: (no net) -> Net-(D70-Pad24)
- D70 pad 26: (no net) -> Net-(D70-Pad26)
- D70 pad 31: (no net) -> Net-(D70-Pad31)
- D70 pad 32: (no net) -> Net-(D70-Pad32)
- D70 pad 36: (no net) -> Net-(D70-Pad36)
- D71 pad 8: (no net) -> Net-(D71-Pad8)
- D74 pad 11: (no net) -> Net-(D74-Pad11)
- D74 pad 12: (no net) -> Net-(D74-Pad12)
- D74 pad 4: (no net) -> Net-(D74-Pad4)
- D74 pad 5: (no net) -> Net-(D74-Pad5)
- D74 pad 6: (no net) -> Net-(D74-Pad6)
- D77 pad 6: (no net) -> Net-(D77-Pad6)
- D79 pad 14: (no net) -> Net-(D79-Pad14)
- D79 pad 15: (no net) -> Net-(D79-Pad15)
- D81 pad 6: (no net) -> Net-(D81-Pad6)
- D88 pad 1: (no net) -> Net-(D88-Pad1)
- D88 pad 2: (no net) -> Net-(D88-Pad2)
- D88 pad 7: (no net) -> Net-(D88-Pad7)
- D88 pad 9: (no net) -> Net-(D88-Pad9)
- D89 pad 11: (no net) -> Net-(D89-Pad11)
- D89 pad 12: (no net) -> Net-(D89-Pad12)
- D89 pad 13: (no net) -> Net-(D89-Pad13)
- D89 pad 7: (no net) -> Net-(D89-Pad7)
- D89 pad 8: (no net) -> Net-(D89-Pad8)
- D89 pad 9: (no net) -> Net-(D89-Pad9)
- X1 pad B20: (no net) -> Net-(X1-PadB20)
- X1 pad B24: (no net) -> /~EXP
- X4 pad A1: (no net) -> Net-(X4-PadA1)
- X4 pad A17: (no net) -> Net-(X4-PadA17)
- X4 pad A2: (no net) -> Net-(X4-PadA2)
- X4 pad A3: (no net) -> Net-(X4-PadA3)
- X4 pad A7: (no net) -> Net-(X4-PadA7)
- X9 pad 10: (no net) -> Net-(X9-Pad10)
- X9 pad 11: (no net) -> Net-(X9-Pad11)
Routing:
- net VCC: track 3431.0 -> 3364.5 mm
- net /HY*: track 119.4 -> 139.0 mm

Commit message: Cosmetic board fixes
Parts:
- added REF**: WireConnection_0-8mmDrill_ThinPad, Wire_Connections_Bridges:WireConnection_0.80mmDrill_ThinPad, F.Cu at (132.3, 98.6)
- added REF**: WireConnection_0-8mmDrill_ThinPad, Wire_Connections_Bridges:WireConnection_0.80mmDrill_ThinPad, F.Cu at (156.0, 108.6)
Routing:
- net /Periphery/TOUT: vias 2 -> 0
- net /Periphery/TIN: vias 2 -> 0
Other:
- outline, holes or cut-outs redrawn
- board text added: "PATISONIC ALESTE 520 EX 01.003"
- board text added: "restored by Alexander Molodtsov, 2015-2017"
- board text removed: "restored by Alexander Molodtsov, 2015"

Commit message: Original board with all fixes
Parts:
- removed the REF** at (52.3, 46.1)
- moved P3 1.25 mm to (237.3, 44.8)
- moved P4 1.25 mm to (234.8, 46.7)
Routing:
- net /WGPTCLK: track 256.8 -> 331.0 mm, vias 5 -> 6
- net /~WAIT: track 36.1 -> 58.2 mm, vias 1 -> 2
- net Net-(D70-Pad25): track 86.6 -> 95.7 mm
- net /D6: track 541.9 -> 548.3 mm
- net Net-(D70-Pad30): track 109.6 -> 114.9 mm
- net Net-(D70-Pad27): track 92.8 -> 98.1 mm
- net /~BUSRQ: track 55.4 -> 60.4 mm
- net /AVCC: track 13.4 -> 18.1 mm
- net Net-(D24-Pad5): track 202.0 -> 206.6 mm
- net /~BUSAK: track 22.5 -> 26.5 mm
- net /D4: track 621.7 -> 625.0 mm
- net GND: track 4144.9 -> 4141.9 mm
- net /AGND: track 15.3 -> 16.5 mm
- net /~ROMEN: track 201.6 -> 200.5 mm
- net /FDC/WRC: track 46.2 -> 47.3 mm
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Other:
- outline, holes or cut-outs redrawn
- board text added: "AGND"
- board text added: "AVCC"
- board text added: "PATISONIC ALESTE 520 EX 01.004"
- board text removed: "PATISONIC ALESTE 520 EX 01.003"
- board text removed: "WGPTCLK"
